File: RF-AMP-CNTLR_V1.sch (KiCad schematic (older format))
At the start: 71 parts, among them J101 VAC, J102 VDC, J103 ext_13V8, J104 Front Panel, J105 ANT_SWITCH, J106 BAND_SELECT, J107 I2C0, J108 VDD_IN, J109 VSS_IN, J110 RELAY RF OUT, J111 RELAY RF IN, J112 FWD3, J113 REF3, J114 FWD4, J115 REF4, J116 PTT, J117 ALC, J118 VDD_AMP, J119 GND_AMP, J120 SPI0, J121 I2C1, J122 RS232, J123 AMP1, J124 AMP2, Q101 DTA124E, U101 KA378R12C, U102 SFH617A-2, U103 L78L33_SOT89

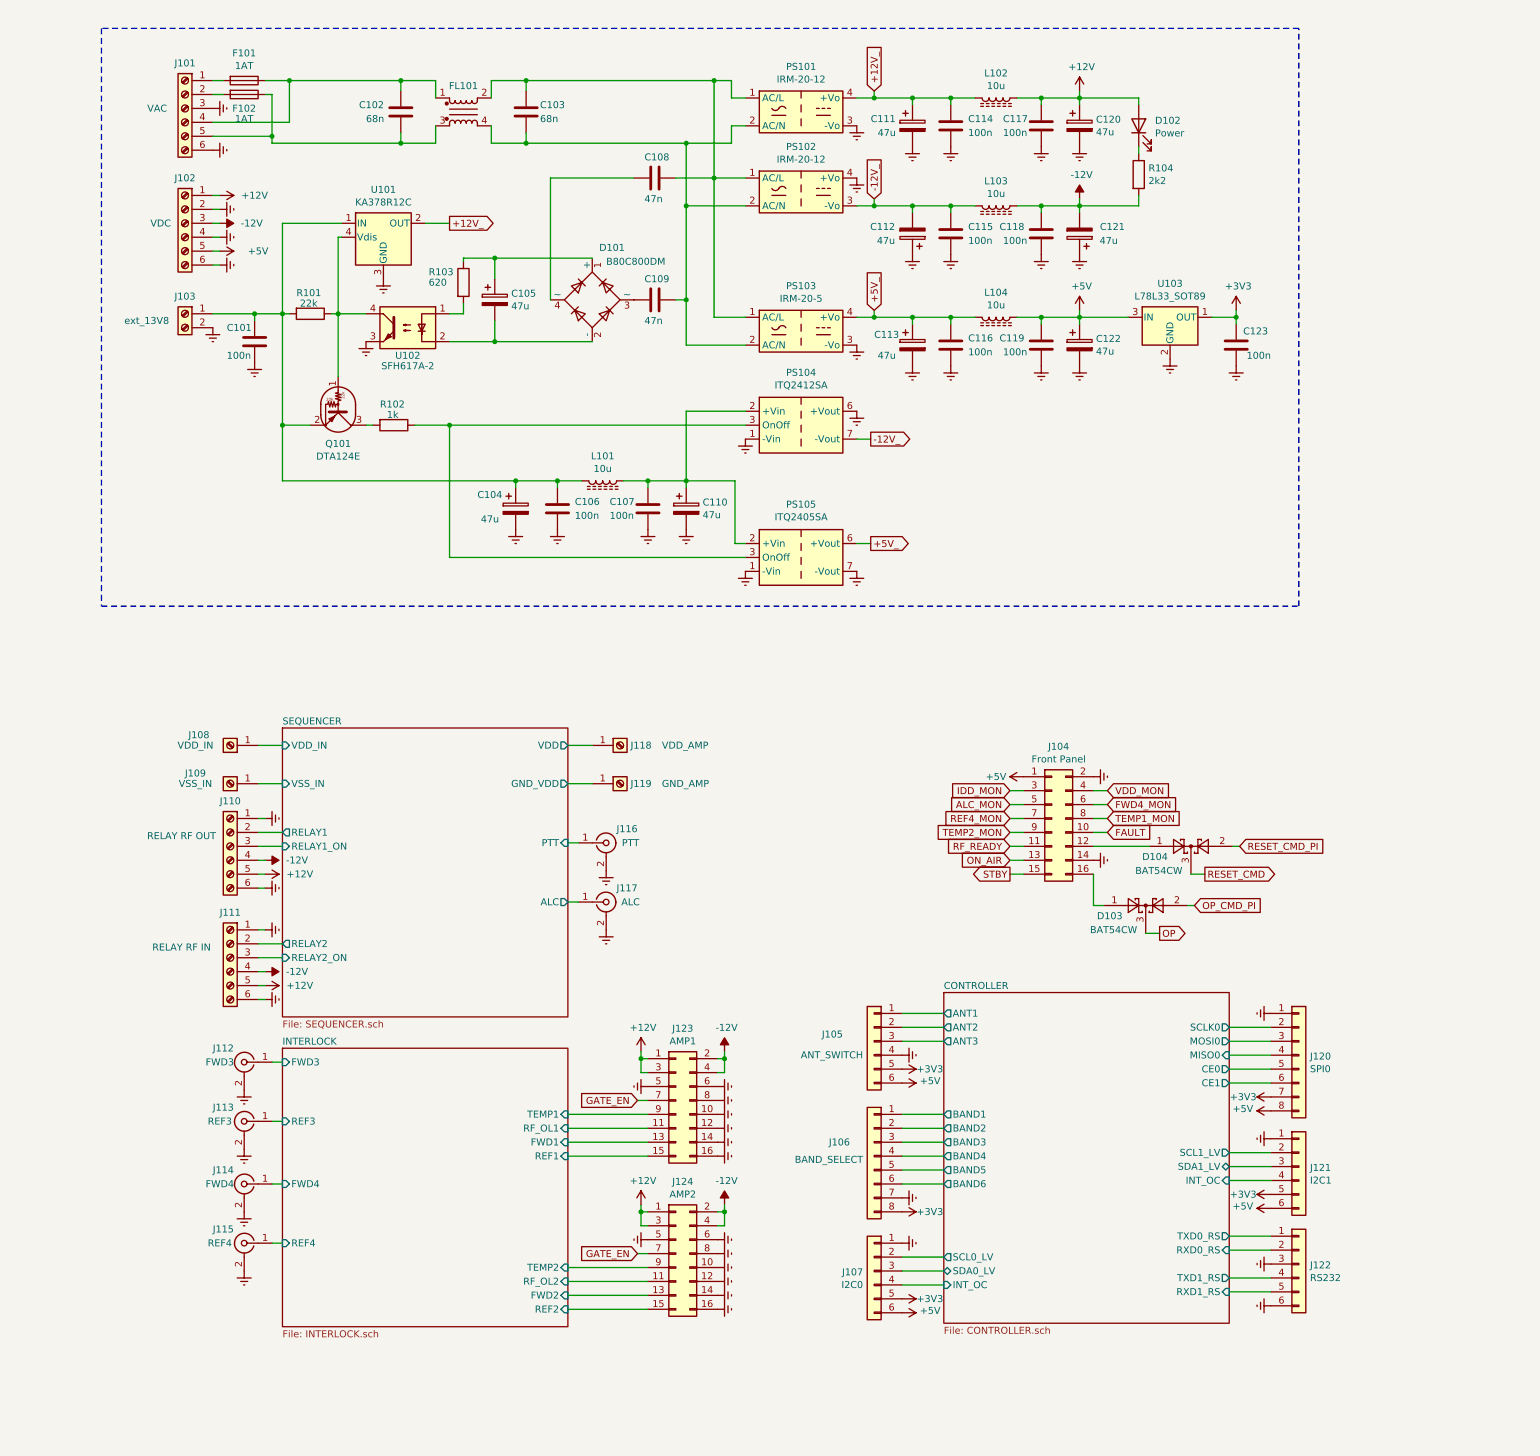
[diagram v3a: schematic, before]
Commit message: new Version with AVR Controller
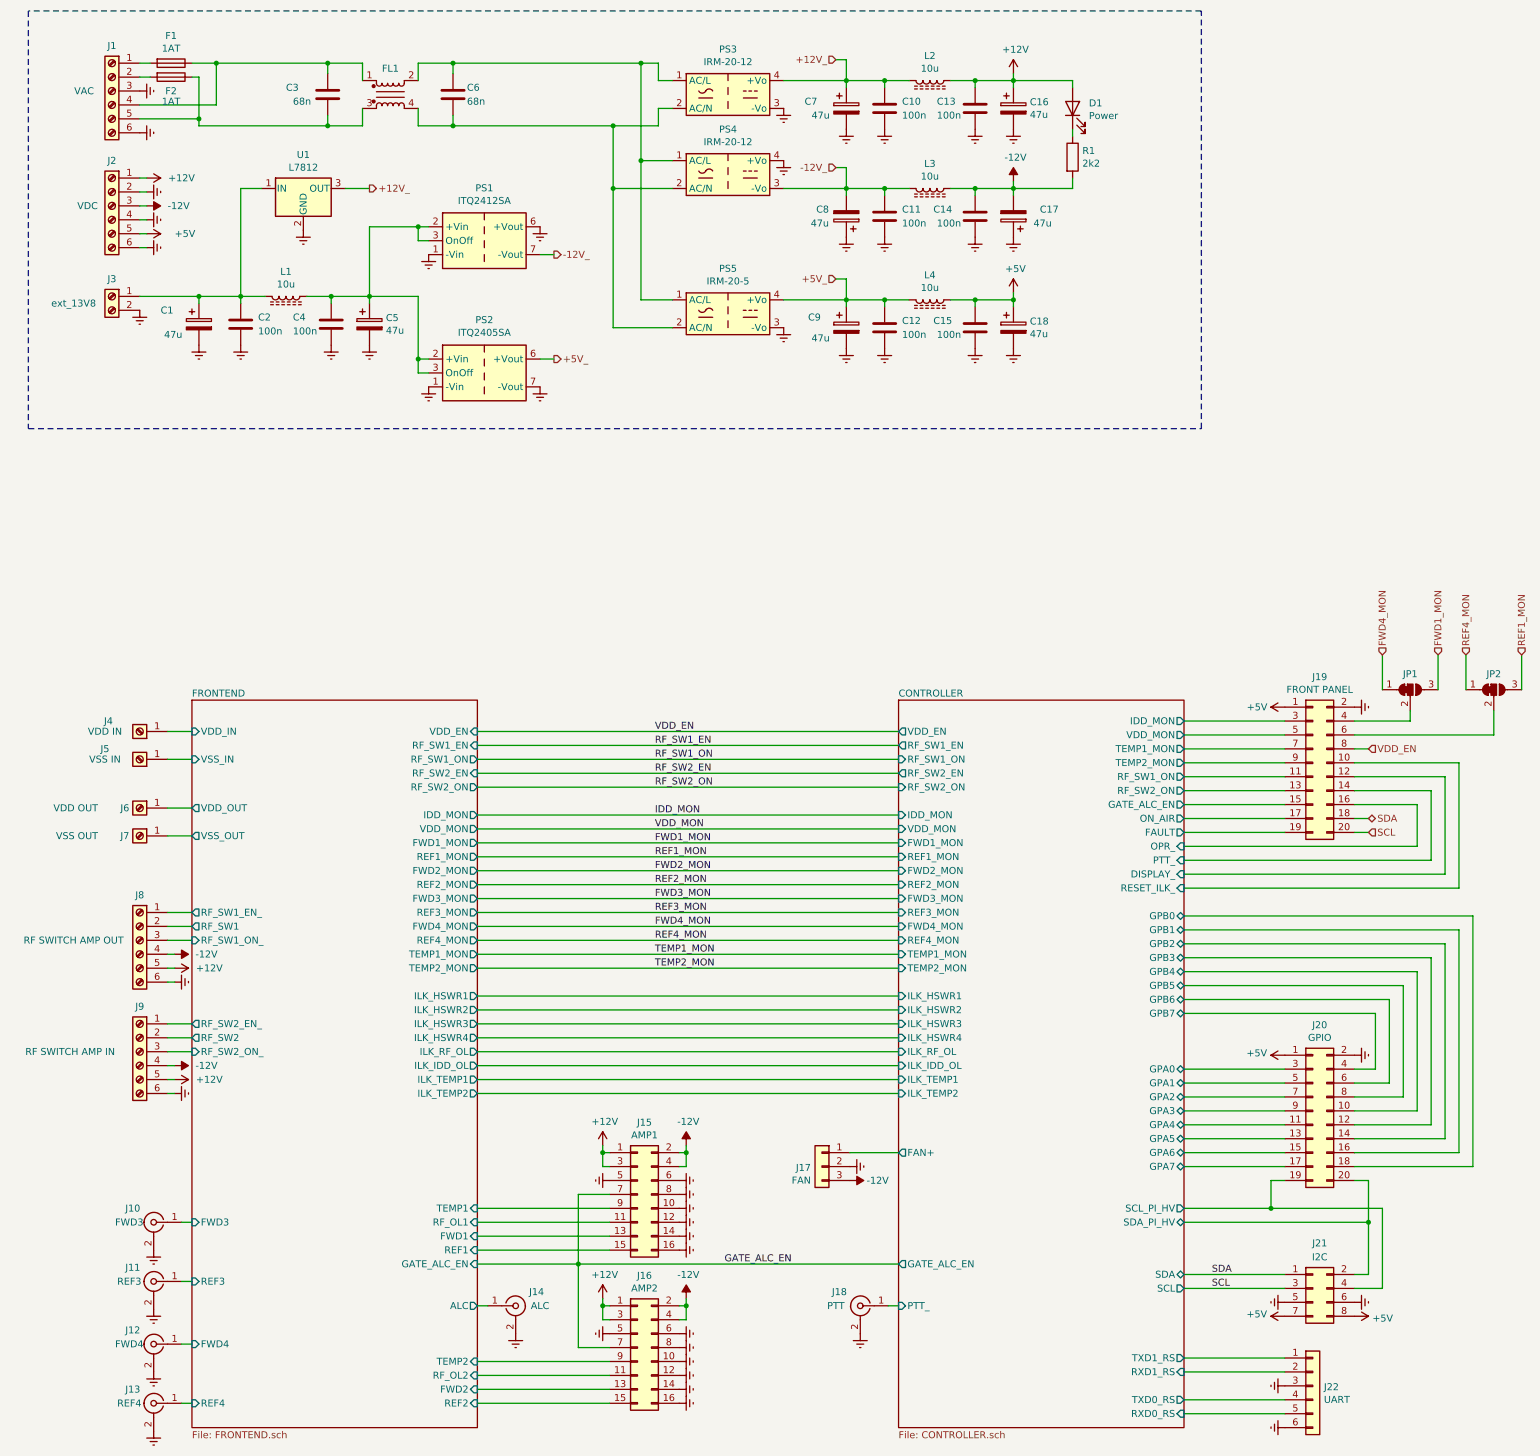
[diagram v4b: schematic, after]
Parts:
- removed C101, C123: 100n, Capacitor_SMD:C_0805_2012Metric_Pad1.15x1.40mm_HandSolder, symbol Device:C
- removed C105: 47u, Capacitor_Tantalum_SMD:CP_EIA-6032-28_Kemet-C, symbol Device:CP
- removed C108, C109: 47n, Capacitor_THT:C_Rect_L7.0mm_W3.5mm_P5.00mm, symbol Device:C
- removed D101: B80C800DM, Diode_THT:Diode_Bridge_DIP-4_W7.62mm_P5.08mm, symbol Diode_Bridge:B80C800DM
- removed D103, D104: BAT54CW, Package_TO_SOT_SMD:SOT-323_SC-70, symbol Diode:BAT54CW
- removed J104: Front Panel, Connector_Multicomp:Multicomp_MC9A12-1634_2x08_P2.54mm_Vertical, symbol Connector_Generic:Conn_02x08_Odd_Even
- removed J105: ANT_SWITCH, Connector_PinHeader_2.54mm:PinHeader_1x06_P2.54mm_Vertical, symbol Connector_Generic:Conn_01x06
- removed J106: BAND_SELECT, Connector_PinHeader_2.54mm:PinHeader_2x04_P2.54mm_Vertical, symbol Connector_Generic:Conn_01x08
- removed J107: I2C0, Connector_PinHeader_2.54mm:PinHeader_1x06_P2.54mm_Vertical, symbol Connector_Generic:Conn_01x06
- removed J120: SPI0, Connector_PinHeader_2.54mm:PinHeader_2x04_P2.54mm_Vertical, symbol Connector_Generic:Conn_01x08
- removed J121: I2C1, Connector_PinHeader_2.54mm:PinHeader_1x06_P2.54mm_Vertical, symbol Connector_Generic:Conn_01x06
- removed Q101: DTA124E, Package_TO_SOT_SMD:SOT-23, symbol Transistor_BJT:DTA124E
- removed R101: 22k, Resistor_SMD:R_0805_2012Metric_Pad1.15x1.40mm_HandSolder, symbol Device:R
- removed R102: 1k, Resistor_SMD:R_0805_2012Metric_Pad1.15x1.40mm_HandSolder, symbol Device:R
- removed R103: 620, Resistor_SMD:R_0805_2012Metric_Pad1.15x1.40mm_HandSolder, symbol Device:R
- removed U101: KA378R12C, Package_TO_SOT_THT:TO-220-4_Vertical, symbol Regulator_Linear:KA378R12C
- removed U102: SFH617A-2, Package_DIP:DIP-4_W7.62mm, symbol Isolator:SFH617A-2
- removed U103: L78L33_SOT89, Package_TO_SOT_SMD:SOT-89-3, symbol Regulator_Linear:L78L33_SOT89
- added J17: FAN, Connector:FanPinHeader_1x03_P2.54mm_Vertical, symbol Connector_Generic:Conn_01x03
- added J19: FRONT PANEL, Connector_Multicomp:Multicomp_MC9A12-2034_2x10_P2.54mm_Vertical, symbol Connector_Generic:Conn_02x10_Odd_Even
- added J20: GPIO, Connector_Multicomp:Multicomp_MC9A12-2034_2x10_P2.54mm_Vertical, symbol Connector_Generic:Conn_02x10_Odd_Even
- added J21: I2C, Connector_PinHeader_2.54mm:PinHeader_2x04_P2.54mm_Vertical, symbol Connector_Generic:Conn_02x04_Odd_Even
- added JP1, JP2: SolderJumper_3_Bridged12, Jumper:SolderJumper-3_P1.3mm_Open_RoundedPad1.0x1.5mm, symbol Jumper:SolderJumper_3_Bridged12
- added U1: L7812, Package_TO_SOT_THT:TO-220-3_Vertical, symbol Regulator_Linear:L7812
- J22: renamed from J122; value RS232 -> UART
- J4: renamed from J108; value VDD_IN -> VDD IN; footprint TerminalBlock_MetzConnect:TerminalBlock_MetzConnect_360425_1x01_Horizontal_ScrewM4.0_Boxed -> footprints-cache:TerminalBlock_MetzConnect_360425_1x01_Horizontal_ScrewM4.0_Boxed
- J5: renamed from J109; value VSS_IN -> VSS IN; footprint TerminalBlock_MetzConnect:TerminalBlock_MetzConnect_360425_1x01_Horizontal_ScrewM4.0_Boxed -> footprints-cache:TerminalBlock_MetzConnect_360425_1x01_Horizontal_ScrewM4.0_Boxed
- J6: renamed from J118; value VDD_AMP -> VDD OUT; footprint TerminalBlock_MetzConnect:TerminalBlock_MetzConnect_360425_1x01_Horizontal_ScrewM4.0_Boxed -> footprints-cache:TerminalBlock_MetzConnect_360425_1x01_Horizontal_ScrewM4.0_Boxed
- J7: renamed from J119; value GND_AMP -> VSS OUT; footprint TerminalBlock_MetzConnect:TerminalBlock_MetzConnect_360425_1x01_Horizontal_ScrewM4.0_Boxed -> footprints-cache:TerminalBlock_MetzConnect_360425_1x01_Horizontal_ScrewM4.0_Boxed
- J8: renamed from J110; value RELAY RF OUT -> RF SWITCH AMP OUT
- J9: renamed from J111; value RELAY RF IN -> RF SWITCH AMP IN
- renumbered C104 to C1, C114 to C10, C115 to C11, C116 to C12, C117 to C13, C118 to C14, C119 to C15, C120 to C16, C121 to C17, C122 to C18, C106 to C2, C102 to C3, C107 to C4, C110 to C5, C103 to C6, C111 to C7, C112 to C8, C113 to C9, D102 to D1, F101 to F1, F102 to F2, FL101 to FL1, J101 to J1, J112 to J10, J113 to J11, J114 to J12, J115 to J13, J117 to J14, J123 to J15, J124 to J16, J116 to J18, J102 to J2, J103 to J3, L101 to L1, L102 to L2, L103 to L3, L104 to L4, PS104 to PS1, PS105 to PS2, PS101 to PS3, PS102 to PS4, PS103 to PS5, R104 to R1
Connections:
- net +12V_: now also U1.3 (OUT)
- net +5V: now also J19.1 (Pin_1), J20.1 (Pin_1), J21.7 (Pin_7), J21.8 (Pin_8)
- net -12V: now also J17.3 (Pin_3)
- net CONTROLLER/RXD0_RS: now also J22.5 (Pin_5); no longer J22.2 (Pin_2)
- net CONTROLLER/RXD1_RS: now also J22.2 (Pin_2); no longer J22.5 (Pin_5)
- net CONTROLLER/TXD0_RS: now also J22.4 (Pin_4); no longer J22.1 (Pin_1)
- net CONTROLLER/TXD1_RS: now also J22.1 (Pin_1); no longer J22.4 (Pin_4)
- net Earth: now also J17.2 (Pin_2), J19.2 (Pin_2), J20.2 (Pin_2), J21.5 (Pin_5), J21.6 (Pin_6), U1.2 (GND); no longer J8.1 (Pin_1), J9.1 (Pin_1)
- net FWD4_MON: now also JP1.1 (A)
- net REF4_MON: now also JP2.1 (A)
- net at C1.1, C2.1, J3.1 (Pin_1)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: now also U1.1 (IN)
- net at C4.1, C5.1, L1.1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: now also PS1.3 (OnOff), PS2.3 (OnOff)
- net GATE_EN renamed GATE_ALC_EN
- net INTERLOCK/FWD1 renamed FRONTEND/FWD1
- net INTERLOCK/FWD2 renamed FRONTEND/FWD2
- net INTERLOCK/FWD3 renamed FRONTEND/FWD3
- net INTERLOCK/FWD4 renamed FRONTEND/FWD4
- net INTERLOCK/REF1 renamed FRONTEND/REF1
- net INTERLOCK/REF2 renamed FRONTEND/REF2
- net INTERLOCK/REF3 renamed FRONTEND/REF3
- net INTERLOCK/REF4 renamed FRONTEND/REF4
- net INTERLOCK/RF_OL1 renamed FRONTEND/RF_OL1
- net INTERLOCK/RF_OL2 renamed FRONTEND/RF_OL2
- net INTERLOCK/TEMP1 renamed FRONTEND/TEMP1
- net INTERLOCK/TEMP2 renamed FRONTEND/TEMP2
- net SEQUENCER/ALC renamed FRONTEND/ALC
- net SEQUENCER/GND_VDD renamed FRONTEND/VSS_OUT
- net SEQUENCER/PTT renamed CONTROLLER/PTT_
- net SEQUENCER/RELAY1 renamed FRONTEND/RF_SW1
- net SEQUENCER/RELAY1_ON renamed FRONTEND/RF_SW1_ON_
- net SEQUENCER/RELAY2 renamed FRONTEND/RF_SW2
- net SEQUENCER/RELAY2_ON renamed FRONTEND/RF_SW2_ON_
- net SEQUENCER/VDD renamed FRONTEND/VDD_OUT
- net SEQUENCER/VDD_IN renamed FRONTEND/VDD_IN
- net SEQUENCER/VSS_IN renamed FRONTEND/VSS_IN
- new net: J19.4 (Pin_4), JP1.2 (C)
- new net: J19.6 (Pin_6), JP2.2 (C)
- new net CONTROLLER/DISPLAY_: J19.12 (Pin_12)
- new net CONTROLLER/FAN+: J17.1 (Pin_1)
- new net CONTROLLER/FAULT: J19.19 (Pin_19)
- new net CONTROLLER/GATE_ALC_EN: J19.15 (Pin_15)
- new net CONTROLLER/GPA0: J20.3 (Pin_3)
- new net CONTROLLER/GPA1: J20.5 (Pin_5)
- new net CONTROLLER/GPA2: J20.7 (Pin_7)
- new net CONTROLLER/GPA3: J20.9 (Pin_9)
- new net CONTROLLER/GPA4: J20.11 (Pin_11)
- new net CONTROLLER/GPA5: J20.13 (Pin_13)
- new net CONTROLLER/GPA6: J20.15 (Pin_15)
- new net CONTROLLER/GPA7: J20.17 (Pin_17)
- new net CONTROLLER/GPB0: J20.18 (Pin_18)
- new net CONTROLLER/GPB1: J20.16 (Pin_16)
- new net CONTROLLER/GPB2: J20.14 (Pin_14)
- new net CONTROLLER/GPB3: J20.12 (Pin_12)
- new net CONTROLLER/GPB4: J20.10 (Pin_10)
- new net CONTROLLER/GPB5: J20.8 (Pin_8)
- new net CONTROLLER/GPB6: J20.6 (Pin_6)
- new net CONTROLLER/GPB7: J20.4 (Pin_4)
- new net CONTROLLER/IDD_MON: J19.3 (Pin_3)
- new net CONTROLLER/ON_AIR: J19.17 (Pin_17)
- new net CONTROLLER/OPR_: J19.16 (Pin_16)
- new net CONTROLLER/PTT_: J19.14 (Pin_14)
- new net CONTROLLER/RESET_ILK_: J19.10 (Pin_10)
- new net CONTROLLER/RF_SW1_ON: J19.11 (Pin_11)
- new net CONTROLLER/RF_SW2_ON: J19.13 (Pin_13)
- new net CONTROLLER/SCL_PI_HV: J20.19 (Pin_19), J21.4 (Pin_4)
- new net CONTROLLER/SDA_PI_HV: J20.20 (Pin_20), J21.2 (Pin_2)
- new net CONTROLLER/TEMP1_MON: J19.7 (Pin_7)
- new net CONTROLLER/TEMP2_MON: J19.9 (Pin_9)
- new net CONTROLLER/VDD_MON: J19.5 (Pin_5)
- new net FRONTEND/RF_SW1_EN_: J8.1 (Pin_1)
- new net FRONTEND/RF_SW2_EN_: J9.1 (Pin_1)
- new net FWD1_MON: JP1.3 (B)
- new net REF1_MON: JP2.3 (B)
- new net SCL: J19.20 (Pin_20), J21.3 (Pin_3)
- new net SDA: J19.18 (Pin_18), J21.1 (Pin_1)
- new net VDD_EN: J19.8 (Pin_8)
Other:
- moved on the sheet: C1, C10, C11, C12, C13, C14, C15, C16, C17, C18, C2, C3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

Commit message: RC2
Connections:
- net CONTROLLER/PTT_ is gone; now on net CONTROLLER/PTT_: J19.14 (Pin_14)
- net CONTROLLER/PTT_: no longer J18.1 (In)
- new net CONTROLLER/PTT_: J18.1 (In)
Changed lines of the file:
@@
 AR Path="/5CBB0B33/5D99E420" Ref="C?"  Part="1"
 AR Path="/5D99E420" Ref="C16"  Part="1"
-F 0 "C16" H 7943 1496 50  0000 L CNN
-F 1 "47u" H 7943 1405 50  0000 L CNN
+F 0 "C16" V 7975 1375 50  0000 L CNN
+F 1 "47u" V 8050 1375 50  0000 L CNN
 F 2 "Capacitor_Tantalum_SMD:CP_EIA-6032-28_Kemet-C" H 7863 1300 50  0001 C CNN
 F 3 "~" H 7825 1450 50  0001 C CNN
@@
 AR Path="/5CBB0B33/5D99E42D" Ref="C?"  Part="1"
 AR Path="/5D99E42D" Ref="C13"  Part="1"
-F 0 "C13" H 7275 1500 50  0000 L CNN
-F 1 "100n" H 7275 1400 50  0000 L CNN
+F 0 "C13" V 7350 1375 50  0000 L CNN
+F 1 "100n" V 7425 1350 50  0000 L CNN
 F 2 "Capacitor_SMD:C_0805_2012Metric_Pad1.15x1.40mm_HandSolder" H 7588 1300 50  0001 C CNN
 F 3 "~" H 7550 1450 50  0001 C CNN
@@
 AR Path="/5CBB0B33/5D99E449" Ref="C?"  Part="1"
 AR Path="/5D99E449" Ref="C10"  Part="1"
-F 0 "C10" H 7025 1500 50  0000 L CNN
-F 1 "100n" H 7025 1400 50  0000 L CNN
+F 0 "C10" V 7025 1375 50  0000 L CNN
+F 1 "100n" V 7100 1350 50  0000 L CNN
 F 2 "Capacitor_SMD:C_0805_2012Metric_Pad1.15x1.40mm_HandSolder" H 6938 1300 50  0001 C CNN
 F 3 "~" H 6900 1450 50  0001 C CNN
@@
 AR Path="/5CBB0B33/5D99E460" Ref="C?"  Part="1"
 AR Path="/5D99E460" Ref="C6"  Part="1"
-F 0 "C6" H 3900 1400 50  0000 L CNN
-F 1 "68n" H 3900 1300 50  0000 L CNN
+F 0 "C6" V 3950 1300 50  0000 L CNN
+F 1 "68n" V 4025 1275 50  0000 L CNN
 F 2 "Capacitor_THT:C_Rect_L13.0mm_W4.0mm_P10.00mm_FKS3_FKP3_MKS4" H 3838 1200 50  0001 C CNN
 F 3 "~" H 3800 1350 50  0001 C CNN
@@
 AR Path="/5CBB0B33/5D99E469" Ref="C?"  Part="1"
 AR Path="/5D99E469" Ref="C3"  Part="1"
-F 0 "C3" H 2600 1400 50  0000 L CNN
-F 1 "68n" H 2650 1300 50  0000 L CNN
+F 0 "C3" V 2675 1300 50  0000 L CNN
+F 1 "68n" V 2750 1275 50  0000 L CNN
 F 2 "Capacitor_THT:C_Rect_L13.0mm_W4.0mm_P10.00mm_FKS3_FKP3_MKS4" H 2938 1200 50  0001 C CNN
 F 3 "~" H 2900 1350 50  0001 C CNN
@@
 AR Path="/5CBB0B33/5D99E5C5" Ref="R?"  Part="1"
 AR Path="/5D99E5C5" Ref="R1"  Part="1"
-F 0 "R1" H 8320 1846 50  0000 L CNN
-F 1 "2k2" H 8320 1755 50  0000 L CNN
+F 0 "R1" V 8350 1750 50  0000 L CNN
+F 1 "2k2" V 8425 1725 50  0000 L CNN
 F 2 "Resistor_SMD:R_0805_2012Metric_Pad1.15x1.40mm_HandSolder" V 8180 1800 50  0001 C CNN
 F 3 "~" H 8250 1800 50  0001 C CNN
@@
 AR Path="/5CBB0B33/5D3E9E7E" Ref="C?"  Part="1"
 AR Path="/5D3E9E7E" Ref="C7"  Part="1"
-F 0 "C7" H 6325 1500 50  0000 L CNN
-F 1 "47u" H 6375 1400 50  0000 L CNN
+F 0 "C7" V 6400 1400 50  0000 L CNN
+F 1 "47u" V 6475 1375 50  0000 L CNN
 F 2 "Capacitor_Tantalum_SMD:CP_EIA-6032-28_Kemet-C" H 6663 1300 50  0001 C CNN
 F 3 "~" H 6625 1450 50  0001 C CNN
@@
 AR Path="/5CBB0B33/5D3F9EE7" Ref="C?"  Part="1"
 AR Path="/5D3F9EE7" Ref="C17"  Part="1"
-F 0 "C17" H 7500 2175 50  0000 L CNN
-F 1 "47u" H 7550 2275 50  0000 L CNN
+F 0 "C17" V 7675 2150 50  0000 L CNN
+F 1 "47u" V 7600 2150 50  0000 L CNN
 F 2 "Capacitor_Tantalum_SMD:CP_EIA-6032-28_Kemet-C" H 7863 2075 50  0001 C CNN
 F 3 "~" H 7825 2225 50  0001 C CNN
@@
 AR Path="/5CBB0B33/5D3F9EF3" Ref="C?"  Part="1"
 AR Path="/5D3F9EF3" Ref="C14"  Part="1"
-F 0 "C14" H 7250 2275 50  0000 L CNN
-F 1 "100n" H 7275 2175 50  0000 L CNN
+F 0 "C14" V 7325 2150 50  0000 L CNN
+F 1 "100n" V 7400 2125 50  0000 L CNN
 F 2 "Capacitor_SMD:C_0805_2012Metric_Pad1.15x1.40mm_HandSolder" H 7588 2075 50  0001 C CNN
 F 3 "~" H 7550 2225 50  0001 C CNN
@@
 AR Path="/5CBB0B33/5D3F9F0D" Ref="C?"  Part="1"
 AR Path="/5D3F9F0D" Ref="C11"  Part="1"
-F 0 "C11" H 7025 2275 50  0000 L CNN
-F 1 "100n" H 7025 2175 50  0000 L CNN
+F 0 "C11" V 7050 2150 50  0000 L CNN
+F 1 "100n" V 7125 2125 50  0000 L CNN
 F 2 "Capacitor_SMD:C_0805_2012Metric_Pad1.15x1.40mm_HandSolder" H 6938 2075 50  0001 C CNN
 F 3 "~" H 6900 2225 50  0001 C CNN
@@
 AR Path="/5CBB0B33/5D3F9F1D" Ref="C?"  Part="1"
 AR Path="/5D3F9F1D" Ref="C8"  Part="1"
-F 0 "C8" H 6750 2175 50  0000 L CNN
-F 1 "47u" H 6750 2275 50  0000 L CNN
+F 0 "C8" V 6850 2175 50  0000 L CNN
+F 1 "47u" V 6775 2150 50  0000 L CNN
 F 2 "Capacitor_Tantalum_SMD:CP_EIA-6032-28_Kemet-C" H 6663 2075 50  0001 C CNN
 F 3 "~" H 6625 2225 50  0001 C CNN
@@
 AR Path="/5CBB0B33/5D586DF5" Ref="C?"  Part="1"
 AR Path="/5D586DF5" Ref="C18"  Part="1"
-F 0 "C18" H 7943 3071 50  0000 L CNN
-F 1 "47u" H 7943 2980 50  0000 L CNN
+F 0 "C18" V 7975 2950 50  0000 L CNN
+F 1 "47u" V 8050 2950 50  0000 L CNN
 F 2 "Capacitor_Tantalum_SMD:CP_EIA-6032-28_Kemet-C" H 7863 2875 50  0001 C CNN
 F 3 "~" H 7825 3025 50  0001 C CNN
@@
 AR Path="/5CBB0B33/5D586E01" Ref="C?"  Part="1"
 AR Path="/5D586E01" Ref="C15"  Part="1"
-F 0 "C15" H 7250 3075 50  0000 L CNN
-F 1 "100n" H 7275 2975 50  0000 L CNN
+F 0 "C15" V 7325 2950 50  0000 L CNN
+F 1 "100n" V 7400 2925 50  0000 L CNN
 F 2 "Capacitor_SMD:C_0805_2012Metric_Pad1.15x1.40mm_HandSolder" H 7588 2875 50  0001 C CNN
 F 3 "~" H 7550 3025 50  0001 C CNN
@@
 AR Path="/5CBB0B33/5D586E2A" Ref="C?"  Part="1"
 AR Path="/5D586E2A" Ref="C9"  Part="1"
-F 0 "C9" H 6350 3100 50  0000 L CNN
-F 1 "47u" H 6375 2950 50  0000 L CNN
+F 0 "C9" V 6400 2975 50  0000 L CNN
+F 1 "47u" V 6475 2950 50  0000 L CNN
 F 2 "Capacitor_Tantalum_SMD:CP_EIA-6032-28_Kemet-C" H 6663 2875 50  0001 C CNN
 F 3 "~" H 6625 3025 50  0001 C CNN
@@
 AR Path="/5CBB0B33/5D59BBDE" Ref="C?"  Part="1"
 AR Path="/5D59BBDE" Ref="C5"  Part="1"
-F 0 "C5" H 3318 3046 50  0000 L CNN
-F 1 "47u" H 3318 2955 50  0000 L CNN
+F 0 "C5" V 3350 2950 50  0000 L CNN
+F 1 "47u" V 3425 2925 50  0000 L CNN
 F 2 "Capacitor_Tantalum_SMD:CP_EIA-6032-28_Kemet-C" H 3238 2850 50  0001 C CNN
 F 3 "~" H 3200 3000 50  0001 C CNN
@@
 AR Path="/5CBB0B33/5D59BBEA" Ref="C?"  Part="1"
 AR Path="/5D59BBEA" Ref="C4"  Part="1"
-F 0 "C4" H 2650 3050 50  0000 L CNN
-F 1 "100n" H 2650 2950 50  0000 L CNN
+F 0 "C4" V 2700 2950 50  0000 L CNN
+F 1 "100n" V 2775 2900 50  0000 L CNN
 F 2 "Capacitor_SMD:C_0805_2012Metric_Pad1.15x1.40mm_HandSolder" H 2963 2850 50  0001 C CNN
 F 3 "~" H 2925 3000 50  0001 C CNN
@@
 AR Path="/5CBB0B33/5D59BC02" Ref="C?"  Part="1"
 AR Path="/5D59BC02" Ref="C2"  Part="1"
-F 0 "C2" H 2400 3050 50  0000 L CNN
-F 1 "100n" H 2400 2950 50  0000 L CNN
+F 0 "C2" V 2425 2950 50  0000 L CNN
+F 1 "100n" V 2500 2900 50  0000 L CNN
 F 2 "Capacitor_SMD:C_0805_2012Metric_Pad1.15x1.40mm_HandSolder" H 2313 2850 50  0001 C CNN
 F 3 "~" H 2275 3000 50  0001 C CNN
@@
 AR Path="/5CBB0B33/5D59BC11" Ref="C?"  Part="1"
 AR Path="/5D59BC11" Ref="C1"  Part="1"
-F 0 "C1" H 1700 3100 50  0000 L CNN
-F 1 "47u" H 1725 2925 50  0000 L CNN
+F 0 "C1" V 1750 2950 50  0000 L CNN
+F 1 "47u" V 1825 2925 50  0000 L CNN
 F 2 "Capacitor_Tantalum_SMD:CP_EIA-6032-28_Kemet-C" H 2013 2850 50  0001 C CNN
 F 3 "~" H 1975 3000 50  0001 C CNN
@@
 AR Path="/5CBB0B33/5D586E1B" Ref="C?"  Part="1"
 AR Path="/5D586E1B" Ref="C12"  Part="1"
-F 0 "C12" H 7025 3075 50  0000 L CNN
-F 1 "100n" H 7025 2975 50  0000 L CNN
+F 0 "C12" V 7050 2950 50  0000 L CNN
+F 1 "100n" V 7125 2925 50  0000 L CNN
 F 2 "Capacitor_SMD:C_0805_2012Metric_Pad1.15x1.40mm_HandSolder" H 6938 2875 50  0001 C CNN
 F 3 "~" H 6900 3025 50  0001 C CNN
